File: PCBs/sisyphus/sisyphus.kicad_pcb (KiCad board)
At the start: 2 copper layers, 60 x 39.5 mm, 65 parts, among them J1 USB_C_Receptacle_USB2.0_14P, J2 AUX USB, J3 Conn_01x02, J4 Speaker, J5 SWD, J6 RGB_CONN, J7 Keyboard, J8 Light sensor, J9 Battery, U1 NCP1117-3.3_SOT223, U2 USBLC6-2P6, U3 W25Q128JVS, U4 MAX98357A, U5 RP2040, U7 BQ25619, Y1 ABM8-272-T3

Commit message: Major PCB update
I won't even bother commenting it
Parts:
- removed C1, C2: 10uF, Capacitor_SMD:C_0805_2012Metric
- removed R9: DNF, Resistor_SMD:R_0402_1005Metric
- removed U1: NCP1117-3.3_SOT223, Package_TO_SOT_SMD:SOT-223-3_TabPin2
- added C20: 100nF, Capacitor_SMD:C_0402_1005Metric, F.Cu at (122.0, 87.1)
- added C26: 10uF, Capacitor_SMD:C_0402_1005Metric, F.Cu at (116.4, 83.7)
- added C27: 10uF, Capacitor_SMD:C_0402_1005Metric, F.Cu at (118.8, 87.7)
- added J10: Limit SW, Connector_PinSocket_2.54mm:PinSocket_1x02_P2.54mm_Vertical, F.Cu at (112.7, 107.5)
- added L7: 2.2uH 1A, Inductor_SMD:L_0603_1608Metric, F.Cu at (118.3, 83.8)
- added Q1: FS8205, Package_TO_SOT_SMD:SOT-23-6, F.Cu at (125.0, 83.5)
- added R16: 100, Resistor_SMD:R_0402_1005Metric, F.Cu at (121.0, 86.1)
- added R17: 1k, Resistor_SMD:R_0402_1005Metric, F.Cu at (123.8, 86.1)
- added U10: TPS62293, Package_SON:WSON-6-1EP_2x2mm_P0.65mm_EP1x1.6mm_ThermalVias, F.Cu at (118.3, 85.9)
- added U8: DW01A, Package_TO_SOT_SMD:SOT-23-6, F.Cu at (121.5, 83.5)
- C15, C17, C22, C24, C25: footprint Capacitor_SMD:C_0805_2012Metric -> Capacitor_SMD:C_0402_1005Metric
- moved H3 38.9 mm to (93.5, 112.9)
- moved J8 38.5 mm to (119.8, 109.8), turned to 90 degrees
- moved H2 38.5 mm to (109.5, 113.5)
- moved H1 33.9 mm to (90.2, 78.5)
- moved H4 30.5 mm to (126.2, 78.3)
- moved J7 16.2 mm to (87.3, 96.2)
- moved J2 12.2 mm to (95.5, 76.8)
- moved R15 10.8 mm to (116.2, 95.0)
- moved TH1 10.8 mm to (114.8, 92.7)
- moved R8 9.80 mm to (108.8, 100.4)
- moved U6 9.43 mm to (94.0, 106.8)
- moved JP2 6.27 mm to (112.8, 100.8), turned to 180 degrees
- moved R6 5.25 mm to (94.3, 95.6)
- moved R3 4.81 mm to (95.3, 95.6)
- moved J4 4.34 mm to (111.2, 93.8)
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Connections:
- C14 pad 2: +3V3 -> VSYS
- C15 pad 2: +3V3 -> VSYS
- J7 pad 1: /COL0 -> /ROW3
- J7 pad 2: /COL1 -> /ROW2
- J7 pad 3: /COL2 -> /ROW1
- J7 pad 4: /COL3 -> /ROW0
- J7 pad 5: /ROW0 -> /COL0
- J7 pad 6: /ROW1 -> /COL1
- J7 pad 7: /ROW2 -> /COL2
- J7 pad 8: /ROW3 -> /COL3
- J9 pad 1: GND -> /B-
- JP2 pad 1: Net-(JP2-A) -> GND
- JP2 pad 2: /GAIN_SELECT -> Net-(JP2-C)
- JP2 pad 3: Net-(JP2-B) -> VSYS
- R8 pad 1: +3V3 -> /GAIN_SELECT
- R8 pad 2: Net-(JP2-B) -> Net-(JP2-C)
- U4 pad 7: +3V3 -> VSYS
- U4 pad 8: +3V3 -> VSYS
- U5 pad 17: unconnected-(U5-GPIO14-Pad17) -> /KEYPAD_INT
- U5 pad 18: unconnected-(U5-GPIO15-Pad18) -> /KEYPAD_RESET
- U5 pad 30: unconnected-(U5-GPIO19-Pad30) -> /LMT_SW
- U5 pad 31: unconnected-(U5-GPIO20-Pad31) -> /AUX_LED
- U5 pad 34: /I2S_ENABLE -> unconnected-(U5-GPIO22-Pad34)
- U5 pad 35: /I2S_DATA -> unconnected-(U5-GPIO23-Pad35)
- U5 pad 36: /I2S_BIT_CLOCK -> /SDA
- U5 pad 37: /I2S_FRAME_CLOCK -> /SCL
- U5 pad 38: unconnected-(U5-GPIO26_ADC0-Pad38) -> /I2S_ENABLE
- U5 pad 39: unconnected-(U5-GPIO27_ADC1-Pad39) -> /I2S_DATA
- U5 pad 40: unconnected-(U5-GPIO28_ADC2-Pad40) -> /I2S_BIT_CLOCK
- U5 pad 41: unconnected-(U5-GPIO29_ADC3-Pad41) -> /I2S_FRAME_CLOCK
- U5 pad 5: /KEYPAD_INT -> unconnected-(U5-GPIO3-Pad5)
- U5 pad 6: /SDA -> unconnected-(U5-GPIO4-Pad6)
- U5 pad 7: /SCL -> unconnected-(U5-GPIO5-Pad7)
- U5 pad 8: /AUX_LED -> unconnected-(U5-GPIO6-Pad8)
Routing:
- net +3V3: track 35.1 -> 111.7 mm, vias 0 -> 12
- net VSYS: track 9.12 -> 30.4 mm, vias 0 -> 5
- net /COL0: track 21.4 -> 4.96 mm
- net /B-: track 0.00 -> 16.0 mm
- net VBUS: track 35.0 -> 19.3 mm
- net /DN: track 30.5 -> 16.4 mm
- net /COL1: track 19.4 -> 5.46 mm
- net /DP: track 29.3 -> 17.1 mm
- net /LMT_SW: track 0.00 -> 11.8 mm
- net /COL2: track 17.4 -> 6.29 mm
- net Net-(U7-TS): track 19.2 -> 8.61 mm
- net /AUX_LED: track 10.6 -> 19.5 mm
- net /GAIN_SELECT: track 9.16 -> 1.23 mm, vias 2 -> 0
- net /COL3: track 15.4 -> 7.99 mm
- net /ROW0: track 13.1 -> 5.79 mm, vias 1 -> 0
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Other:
- board size 60 x 39.5 mm -> 52 x 42 mm
- board text added: "BAT"
- board text added: "BAT TEMP"
- board text added: "CLANG!"
- board text added: "CLR SENS"
- board text added: "GAIN SLCT"
- board text added: "KBD"
- board text added: "LMT SW"
- board text added: "Made with by Plajta"
- board text added: "Sisyfoss"
- board text added: "β"
- board text removed: "KEYBOARD"
- board text removed: "Made by Plajta"
- board text removed: "Sisyphus v0.1"

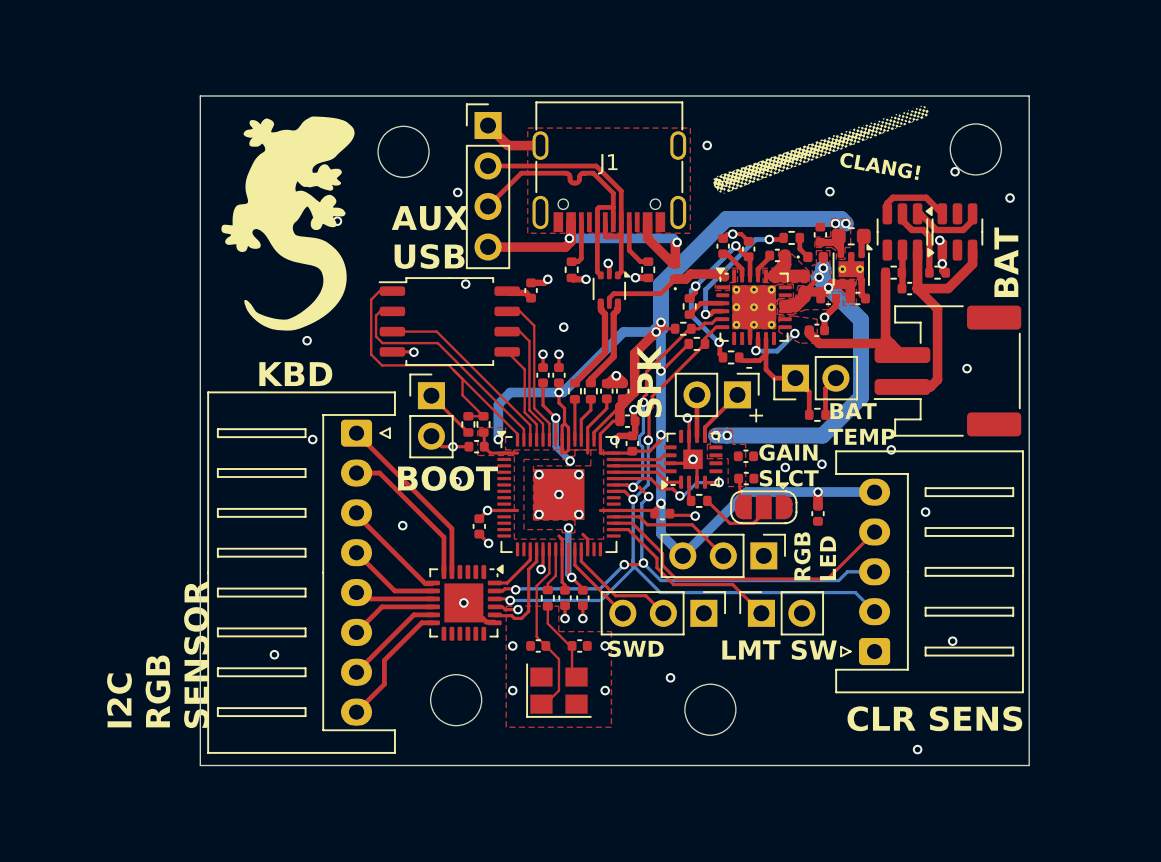
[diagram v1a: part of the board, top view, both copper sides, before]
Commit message: Fix critical PCB errors
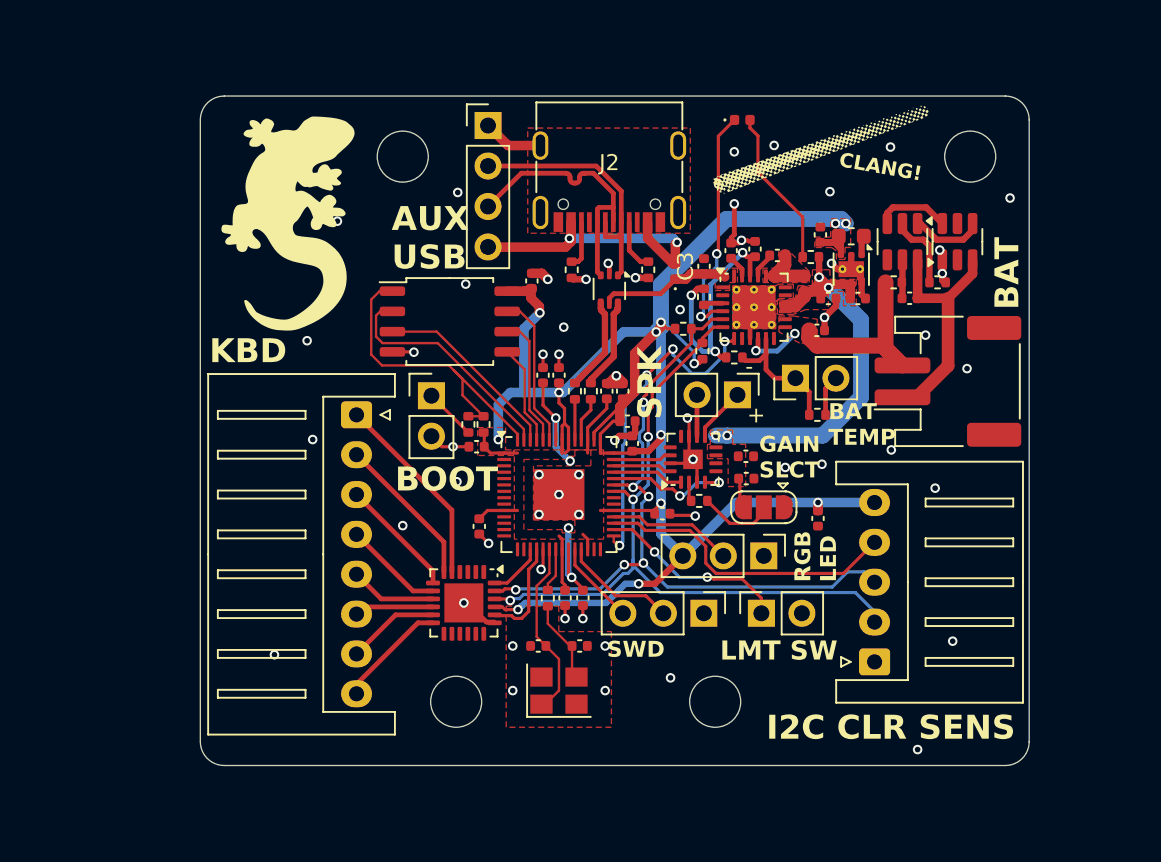
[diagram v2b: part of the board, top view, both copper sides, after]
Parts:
- added C3: 1uF, Capacitor_SMD:C_0402_1005Metric, F.Cu at (109.1, 85.7)
- moved D2 9.75 mm to (111.5, 76.5)
- moved R3 1.70 mm to (115.8, 85.1)
- moved J10 1.15 mm to (87.3, 95.0)
- moved R4 1.08 mm to (109.1, 87.6)
- moved J1 0.65 mm to (119.8, 110.5)
- moved J6 0.65 mm to (124.4, 92.9)
- moved C25 0.61 mm to (122.0, 87.7)
- moved Q1 0.61 mm to (125.0, 84.1)
- moved R15 0.61 mm to (121.0, 86.7)
- moved R16 0.61 mm to (123.8, 86.7)
- moved U6 0.61 mm to (121.5, 84.1)
- moved C11 0.60 mm to (98.3, 86.6)
- moved H2 0.58 mm to (109.8, 113.0)
- moved C8 0.57 mm to (110.8, 84.7)
- moved H4 0.57 mm to (125.8, 78.8)
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- renumbered C21 to C1, C15 to C10, C16 to C11, C3 to C12, C4 to C13, C5 to C14, C6 to C15, C7 to C16, C8 to C17, C9 to C18, C10 to C19, C22 to C2, C11 to C20, C12 to C21, C13 to C22, C18 to C23, C19 to C24, C20 to C25, C17 to C26, C27 to C4, C26 to C5, C24 to C6, C23 to C7, C25 to C8, C14 to C9, J8 to J1, J7 to J10, J1 to J2, J2 to J3, J3 to J4, J4 to J5, J9 to J6, J5 to J7, J10 to J8, J6 to J9, JP2 to JP1, L7 to L2, R4 to R10, R5 to R11, R10 to R12, R11 to R13, R7 to R14, R16 to R15, R17 to R16, R12 to R3, R13 to R4, R14 to R5, R15 to R6, R3 to R7, R6 to R8, R8 to R9, U10 to U1, U7 to U3, U3 to U4, U4 to U5, U8 to U6, U5 to U7, U6 to U8
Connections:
- D2 pad 2: VSYS -> Net-(D2-A)
- R3 pad 1: Net-(U7-STAT) -> Net-(D2-A)
- R3 pad 2: Net-(D2-K) -> VSYS
- U3 pad 4: Net-(U7-STAT) -> Net-(D2-K)
- U7 pad 29: unconnected-(U5-GPIO18-Pad29) -> /PMIC_INT
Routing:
- net /PMIC_INT: track 0.00 -> 20.6 mm, vias 0 -> 4
- net +3V3: track 111.7 -> 131.5 mm, vias 12 -> 13
- net Net-(D2-K): track 1.41 -> 14.7 mm, vias 0 -> 2
- net Net-(D2-A): track 0.00 -> 9.97 mm
- net Net-(U7-STAT): track 8.94 -> 0.00 mm, vias 2 -> 0
- net /REGN: track 12.3 -> 15.9 mm
- net GND: track 44.4 -> 47.6 mm, vias 53 -> 57
- net VSYS: track 30.4 -> 28.8 mm, vias 5 -> 4
- net +BATT: track 14.9 -> 16.5 mm
- net /ROW3: track 11.2 -> 12.3 mm
- net Net-(U3-PMID_GOOD): track 2.37 -> 1.22 mm
- net /COL3: track 7.99 -> 6.99 mm
- net /ROW1: track 6.67 -> 7.54 mm
- net /SDA: track 45.4 -> 46.1 mm
- net /B-: track 16.0 -> 15.3 mm
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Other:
- outline, holes or cut-outs redrawn
- board text added: "Ano, prosím, ještě víc!"
- board text added: "I2C CLR SENS"
- board text added: "SisypFOSS"
- board text removed: "CLR SENS"
- board text removed: "I2C RGB SENSOR"
- board text removed: "Sisyfoss"

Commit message: Add some ✨flair✨ to the PCB
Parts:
- H1, H2, H3, H4: footprint MountingHole:MountingHole_3.2mm_M3_ISO7380 -> MountingHole:MountingHole_3.2mm_M3_ISO7380_Pad
- moved H2 39.4 mm to (90.2, 78.8)
- moved H4 38.1 mm to (109.0, 113.0)
- moved H1 35.6 mm to (125.8, 78.8)
- moved H3 0.10 mm to (93.5, 113.0)
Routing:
- net GND: vias 57 -> 56
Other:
- board text added: "Ano, prosím"
- board text added: "Ještě víc!"
- board text added: "SisyFOSS"
- board text removed: "Ano, prosím, ještě víc!"
- board text removed: "SisypFOSS"

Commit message: Add power switch
Minor changes
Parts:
- added Q1: AO3401A, Package_TO_SOT_SMD:SOT-23, F.Cu at (117.8, 85.5)
- added R1: 1M, Resistor_SMD:R_0402_1005Metric, F.Cu at (116.8, 87.7)
- added SW1: SW_SPDT_321, Connector_PinHeader_2.54mm:PinHeader_1x03_P2.54mm_Vertical, F.Cu at (119.7, 77.2)
- J4: value Conn_01x02 -> USB_BOOT
- moved C4 5.22 mm to (116.8, 82.8), turned to 90 degrees
- moved L2 3.43 mm to (118.6, 80.4)
- moved U1 3.43 mm to (118.6, 82.4)
- moved J4 3.40 mm to (92.0, 97.2), turned to 180 degrees
- moved C5 2.71 mm to (116.7, 81.0), turned to -90 degrees
- moved J8 2.50 mm to (115.2, 107.5), turned to -90 degrees
- moved C2 1.45 mm to (115.8, 88.7)
- moved R4 0.99 mm to (115.3, 84.2), turned to -90 degrees
- moved J1 0.70 mm to (119.8, 111.2)
- moved L1 0.05 mm to (115.3, 86.8)
- renumbered Q1 to Q2, R9 to R10, R10 to R11, R11 to R12, R12 to R13, R13 to R14, R14 to R15, R15 to R16, R16 to R17, R1 to R2, R2 to R3, R3 to R4, R4 to R5, R5 to R6, R6 to R7, R7 to R8, R8 to R9
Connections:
- C2 pad 1: VSYS -> SYS
- J4 pad 1: /~{USB_BOOT} -> GND
- J4 pad 2: GND -> /~{USB_BOOT}
- J8 pad 1: /LMT_SW -> GND
- J8 pad 2: GND -> /LMT_SW
- L1 pad 2: VSYS -> SYS
- R4 pad 2: VSYS -> SYS
- U3 pad 15: VSYS -> SYS
- U3 pad 16: VSYS -> SYS
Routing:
- net Net-(Q1-G): track 0.00 -> 12.5 mm, vias 0 -> 1
- net VSYS: track 28.8 -> 19.4 mm, vias 4 -> 5
- net SYS: track 0.00 -> 8.74 mm
- net +3V3: track 131.5 -> 130.4 mm, vias 13 -> 14
- net GND: track 47.6 -> 47.2 mm, vias 56 -> 53
- added copper zone on F.Cu, net SYS
- added copper zone on B.Cu, net VSYS
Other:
- board text added: "ON"

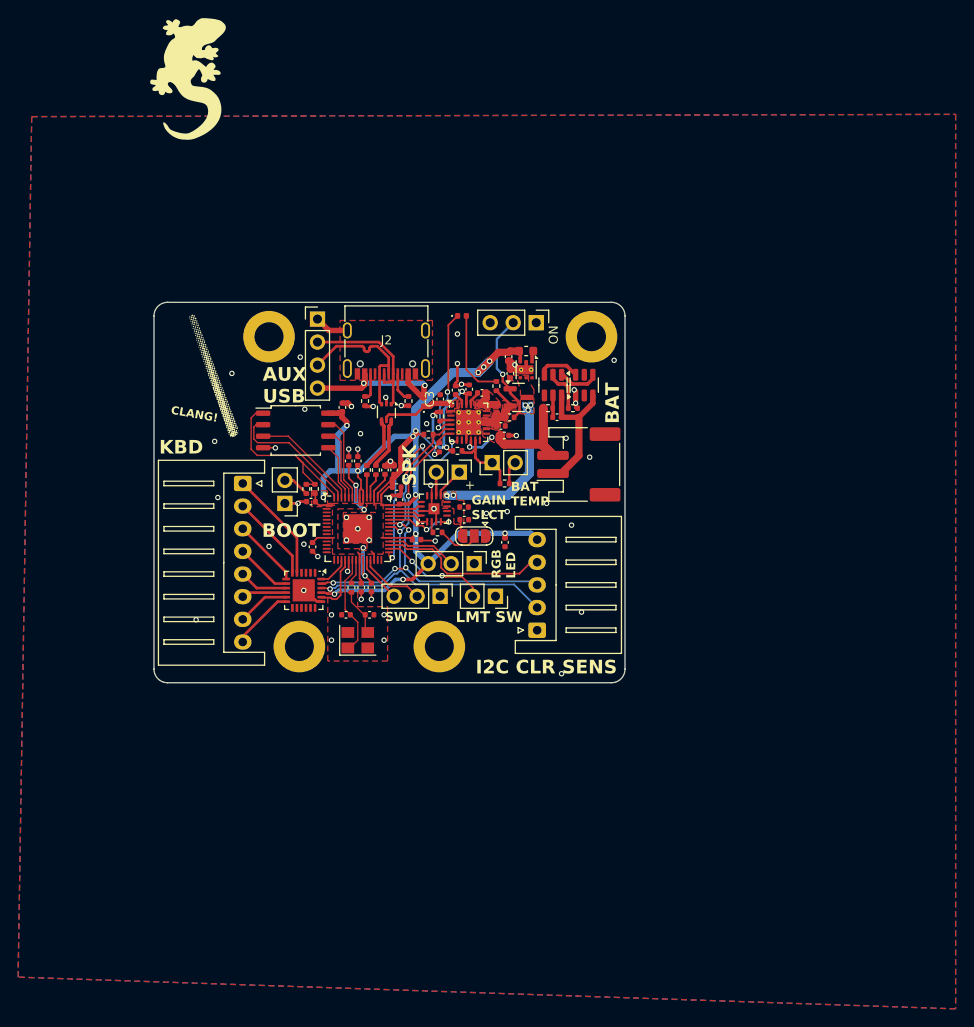
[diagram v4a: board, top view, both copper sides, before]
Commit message: Some schematic readability improved. Minor changes in PCB
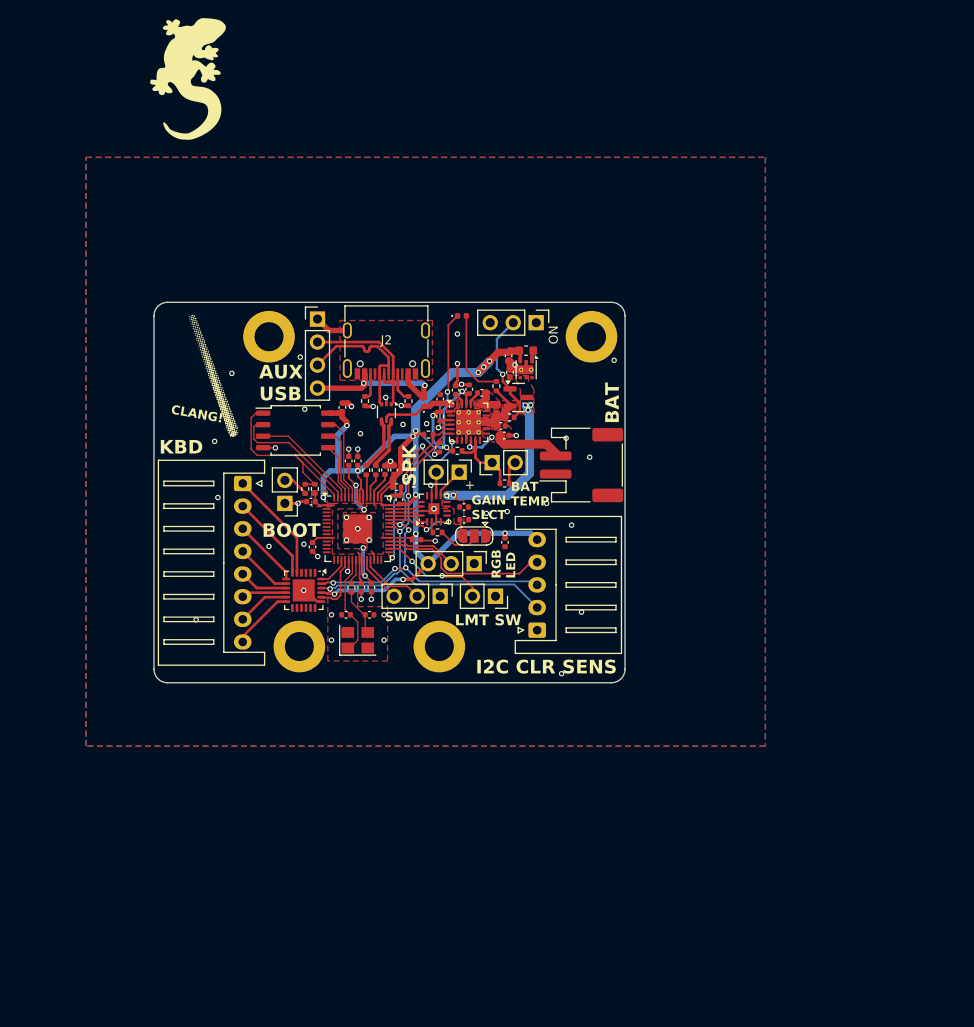
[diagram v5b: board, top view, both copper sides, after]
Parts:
- removed C25: 100nF, Capacitor_SMD:C_0402_1005Metric
- removed Q2: FS8205, Package_TO_SOT_SMD:SOT-23-6
- removed R16: 100, Resistor_SMD:R_0402_1005Metric
- removed R17: 1k, Resistor_SMD:R_0402_1005Metric
- removed U6: DW01A, Package_TO_SOT_SMD:SOT-23-6
- moved J6 0.30 mm to (124.7, 93.0)
- moved C4 0.12 mm to (116.8, 82.7)
- moved R9 0.12 mm to (94.2, 95.6)
- moved C5 0.09 mm to (116.6, 80.9)
- moved R11 0.07 mm to (100.9, 93.5)
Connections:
- net /AUX_LED renamed AUX_LED
- net /COL0 renamed /Peripheral/COL0
- net /COL1 renamed /Peripheral/COL1
- net /COL2 renamed /Peripheral/COL2
- net /COL3 renamed /Peripheral/COL3
- net /DN renamed /Peripheral/DN
- net /DP renamed /Peripheral/DP
- net /GAIN_SELECT renamed /Peripheral/GAIN_SELECT
- net /I2S_BIT_CLOCK renamed I2S_BIT_CLOCK
- net /I2S_DATA renamed I2S_DATA
- net /I2S_ENABLE renamed I2S_ENABLE
- net /I2S_FRAME_CLOCK renamed I2S_FRAME_CLOCK
- net /KEYPAD_INT renamed KEYPAD_INT
- net /KEYPAD_RESET renamed KEYPAD_RESET
- net /LMT_SW renamed LMT_SW
- net /PMIC_INT renamed PMIC_INT
- net /REGN renamed /Batery and power/REGN
- net /RGB_DATA renamed RGB_DATA
- net /ROW0 renamed /Peripheral/ROW0
- net /ROW1 renamed /Peripheral/ROW1
- net /ROW2 renamed /Peripheral/ROW2
- net /ROW3 renamed /Peripheral/ROW3
- net /SCL renamed SCL
- net /SDA renamed SDA
- net /SPK+ renamed /Peripheral/SPK+
- net /SPK- renamed /Peripheral/SPK-
- net /SW renamed /Batery and power/SW
- net /USB_D+ renamed USB_D+
- net /USB_D- renamed USB_D-
- net /XIN renamed Net-(U7-XIN)
- net /XOUT renamed Net-(U7-XOUT)
- J6 pad 1: /B- -> GND
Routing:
- net /B-: track 15.3 -> 0.00 mm
- net +BATT: track 16.5 -> 11.2 mm
- net /CS: track 4.81 -> 0.00 mm
- net /OC: track 4.68 -> 0.00 mm
- net /OD: track 4.54 -> 0.00 mm
- net Net-(U6-VCC): track 2.42 -> 0.00 mm
- net GND: track 47.2 -> 45.8 mm, vias 53 -> 52
